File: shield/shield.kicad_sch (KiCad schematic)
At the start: 34 parts, among them Q1 Q_NMOS_DSG, Q2 Q_NMOS_DSG, U1 LM74900

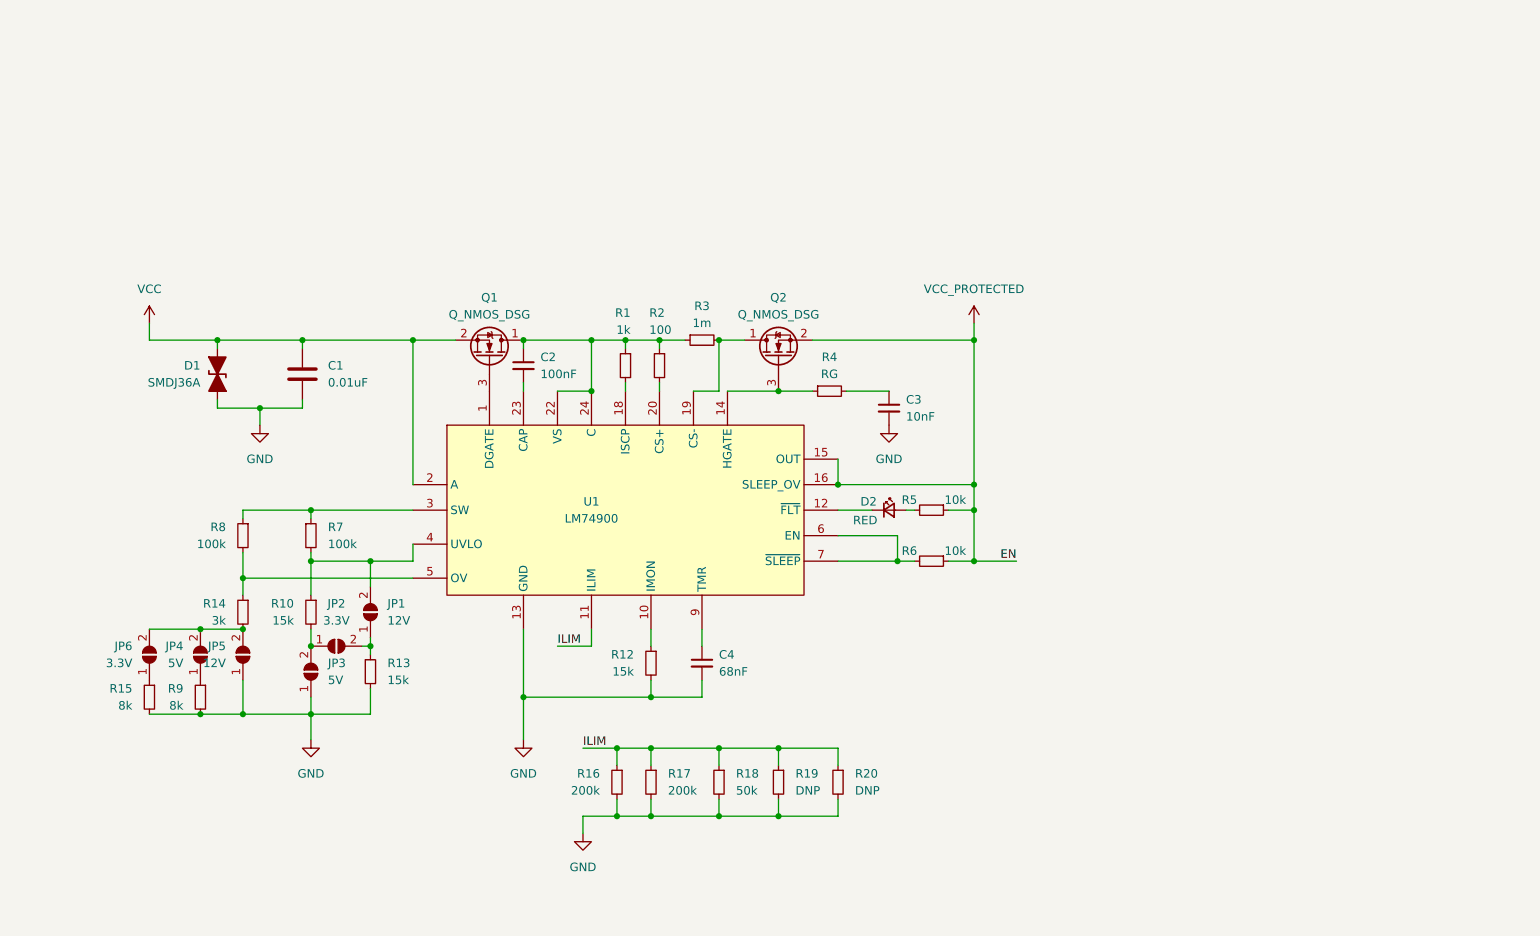
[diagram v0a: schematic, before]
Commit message: Feat[shield]: initial board layout + temporary footprints
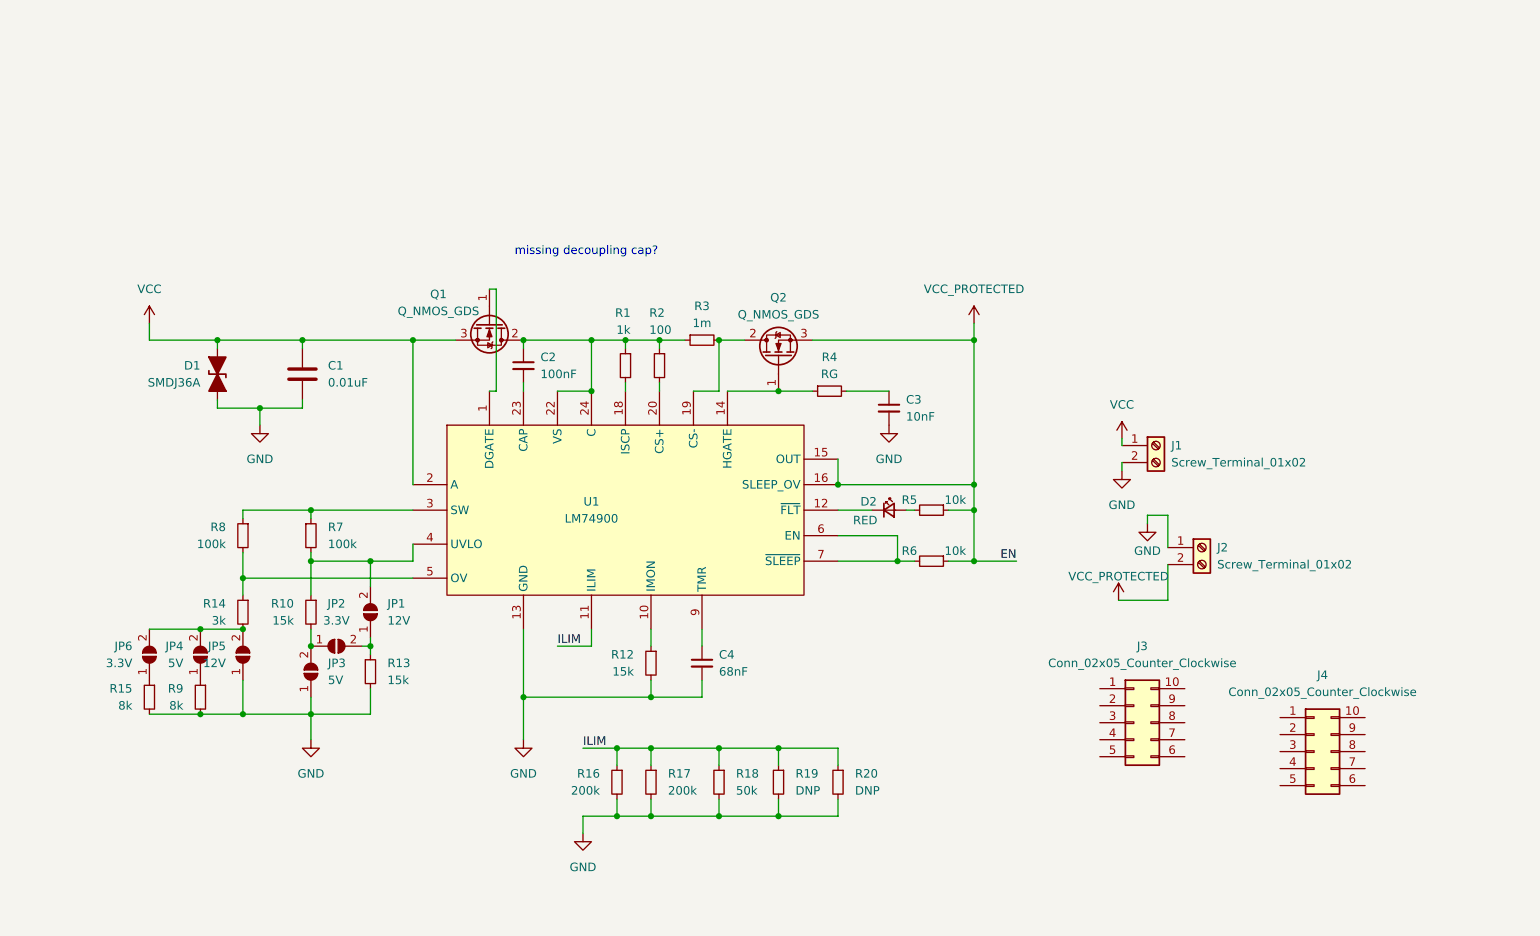
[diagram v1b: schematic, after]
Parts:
- removed Q1, Q2: Q_NMOS_DSG, symbol Device:Q_NMOS_DSG
- added J1, J2: Screw_Terminal_01x02, TerminalBlock_Phoenix:TerminalBlock_Phoenix_MKDS-1,5-2-5.08_1x02_P5.08mm_Horizontal, symbol Connector:Screw_Terminal_01x02
- added J3: Conn_02x05_Counter_Clockwise, DF40C-10:CONN_DF40B-10DS-0.4V51_HIR, symbol Connector_Generic:Conn_02x05_Counter_Clockwise
- added J4: Conn_02x05_Counter_Clockwise, DF40C-10:CONN_DF40C-10DP-0.4V51_HIR, symbol Connector_Generic:Conn_02x05_Counter_Clockwise
- added Q1, Q2: Q_NMOS_GDS, Package_TO_SOT_SMD:Infineon_PG-HSOF-8-1_ThermalVias, symbol Device:Q_NMOS_GDS
- C1, C2, C3, C4: footprint (none) -> Capacitor_SMD:C_0603_1608Metric
- D1: footprint (none) -> Diode_SMD:D_SMC
- D2: footprint (none) -> Diode_SMD:D_0603_1608Metric
- JP1, JP2, JP3, JP4, JP5, JP6: footprint (none) -> Jumper:SolderJumper-2_P1.3mm_Open_Pad1.0x1.5mm
- R1, R10, R12, R13, R14, R15, R16, R17, R18, R19, R2, R20, R4, R5, R6, R7, R8, R9: footprint (none) -> Resistor_SMD:R_0603_1608Metric
- R3: footprint (none) -> Resistor_SMD:R_2512_6332Metric
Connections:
- net GND: now also J1.2 (Pin_2), J2.1 (Pin_1)
- net VCC: now also J1.1 (Pin_1), Q1.3 (S)
- net VCC_PROTECTED: now also J2.2 (Pin_2), Q2.3 (S)
- net at C2.1, R1.1, R2.1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: now also Q1.2 (D)
- net at U1.1 (DGATE): now also Q1.1 (G)
- net at R3.2, U1.19 (CS-): now also Q2.2 (D)
- net at R4.1, U1.14 (HGATE): now also Q2.1 (G)
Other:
- note added: "missing decoupling cap?"

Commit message: Feat(shield): ready for routing
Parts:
- removed D2: RED, Diode_SMD:D_0603_1608Metric, symbol Device:LED_Small
- removed J3: Conn_02x05_Counter_Clockwise, DF40C-10:CONN_DF40B-10DS-0.4V51_HIR, symbol Connector_Generic:Conn_02x05_Counter_Clockwise
- removed J4: Conn_02x05_Counter_Clockwise, DF40C-10:CONN_DF40C-10DP-0.4V51_HIR, symbol Connector_Generic:Conn_02x05_Counter_Clockwise
- removed Q1, Q2: Q_NMOS_GDS, Package_TO_SOT_SMD:Infineon_PG-HSOF-8-1_ThermalVias, symbol Device:Q_NMOS_GDS
- added J3: IC Side 1, Connector_PinHeader_2.54mm:PinHeader_1x04_P2.54mm_Vertical, symbol Connector_Generic:Conn_01x04
- added J4: IC Side 2, Connector_PinHeader_2.54mm:PinHeader_1x04_P2.54mm_Vertical, symbol Connector_Generic:Conn_01x04
- added J5: Power Side 1, Connector_PinHeader_2.54mm:PinHeader_1x04_P2.54mm_Vertical, symbol Connector_Generic:Conn_01x04
- added J6: Power Side 2, Connector_PinHeader_2.54mm:PinHeader_1x04_P2.54mm_Vertical, symbol Connector_Generic:Conn_01x04
- added Q1, Q2: GAN3R2-100CBE, WLCSP8-SOT8072:WLCSP8-SOT8072, symbol NFET:Q_NMOS_GSD
- added TP1: ~{FLT}, TestPoint:TestPoint_Pad_1.0x1.0mm, symbol Connector:TestPoint_Small
- added TP2: EN, TestPoint:TestPoint_Pad_1.0x1.0mm, symbol Connector:TestPoint_Small
- added TP3: ~{SLEEP}, TestPoint:TestPoint_Pad_1.0x1.0mm, symbol Connector:TestPoint_Small
- C1: value 0.01uF -> 0.1uF; footprint Capacitor_SMD:C_0603_1608Metric -> Capacitor_SMD:C_1206_3216Metric
- JP1: value 12V -> 6
- JP2: value 3.3V -> 5
- JP3: value 5V -> 4
- JP4: value 5V -> 2
- JP5: value 12V -> 3
- JP6: value 3.3V -> 1
- R1, R10, R12, R13, R14, R15, R16, R17, R18, R2, R4, R5, R6, R7, R8, R9: footprint Resistor_SMD:R_0603_1608Metric -> Resistor_SMD:R_0402_1005Metric
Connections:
- net GND: now also J3.4 (Pin_4), J4.4 (Pin_4), J5.4 (Pin_4), J6.4 (Pin_4)
- net VCC: now also J5.1 (Pin_1), Q1.S; no longer U1.2 (A)
- net VCC_PROTECTED: now also J6.3 (Pin_3), Q2.S; no longer R5.1, R6.1, U1.15 (OUT), U1.16 (SLEEP_OV)
- net GATE1_IC: now reaches U1.1 (DGATE)
- net GATE1_IC: now also J3.2 (Pin_2)
- net SHUNT+_IC: now reaches C2.1, R1.1, R2.1, U1.22 (VS), U1.24 (C)
- net SHUNT+_IC: now also J3.3 (Pin_3); no longer R3.1
- net GATE2_IC: now reaches R4.1, U1.14 (HGATE)
- net GATE2_IC: now also J4.2 (Pin_2)
- net SHUNT-_IC: now reaches U1.19 (CS-)
- net SHUNT-_IC: now also J4.1 (Pin_1); no longer R3.2
- net at R6.2, U1.6 (EN), U1.7 (~{SLEEP}): now also TP2.1, TP3.1
- net at U1.12 (~{FLT}): now also R5.2, TP1.1
- new net EN: J4.3 (Pin_3), R5.1, R6.1, U1.15 (OUT), U1.16 (SLEEP_OV)
- new net GATE1_PWR: J5.2 (Pin_2), Q1.G
- new net GATE2_PWR: J6.2 (Pin_2), Q2.G
- new net SHUNT+_PWR: J5.3 (Pin_3), Q1.D, R3.1
- new net SHUNT-_PWR: J6.1 (Pin_1), Q2.D, R3.2
- new net VCC_IC: J3.1 (Pin_1), U1.2 (A)
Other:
- note added: "missing decoupling cap? - max"
- note added: "what do you mean? - byran"
- note removed: "missing decoupling cap?"
- moved on the sheet: C1, D1, J1, J2, R3

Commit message: Feat(shield): initial routing
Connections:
- net EN: now also J4.4 (Pin_4); no longer J4.3 (Pin_3)
- net GATE1_IC: now also J4.1 (Pin_1); no longer J3.2 (Pin_2)
- net GATE1_PWR: now also J6.1 (Pin_1); no longer J5.2 (Pin_2)
- net GATE2_IC: now also J3.3 (Pin_3); no longer J4.2 (Pin_2)
- net GATE2_PWR: now also J5.3 (Pin_3); no longer J6.2 (Pin_2)
- net GND: now also J3.2 (Pin_2), J5.2 (Pin_2); no longer J4.4 (Pin_4), J6.4 (Pin_4)
- net SHUNT+_IC: now also J4.2 (Pin_2); no longer J3.3 (Pin_3)
- net SHUNT+_PWR: now also J6.2 (Pin_2); no longer J5.3 (Pin_3)
- net SHUNT-_IC: now also J4.3 (Pin_3); no longer J4.1 (Pin_1)
- net SHUNT-_PWR: now also J6.3 (Pin_3); no longer J6.1 (Pin_1)
- net VCC_PROTECTED: now also J6.4 (Pin_4); no longer J6.3 (Pin_3)
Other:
- note added: "100nF for VS pin - Max"
- moved on the sheet: J4, J5
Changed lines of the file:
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@@
 	(wire
 		(pts
-			(xy 179.07 151.13) (xy 193.04 151.13)
+			(xy 179.07 137.16) (xy 193.04 137.16)
 		)
 		(stroke
@@
 	(wire
 		(pts
-			(xy 179.07 137.16) (xy 193.04 137.16)
+			(xy 179.07 156.972) (xy 193.04 156.972)
 		)
 		(stroke
@@
 	(wire
 		(pts
+			(xy 216.916 136.652) (xy 235.966 136.652)
+		)
+		(stroke
+			(width 0)
+			(type default)
+		)
+	)
+	(wire
+		(pts
 			(xy 88.9 134.62) (xy 88.9 133.35)
 		)
@@
 	(wire
 		(pts
-			(xy 212.09 151.13) (xy 227.33 151.13)
+			(xy 220.726 139.192) (xy 235.966 139.192)
 		)
 		(stroke
@@
 	(wire
 		(pts
-			(xy 212.09 148.59) (xy 227.33 148.59)
+			(xy 216.408 158.75) (xy 231.648 158.75)
 		)
 		(stroke
@@
 	(wire
 		(pts
-			(xy 212.09 137.16) (xy 227.33 137.16)
+			(xy 216.408 156.21) (xy 231.648 156.21)
 		)
 		(stroke
@@
 	(wire
 		(pts
-			(xy 212.09 153.67) (xy 227.33 153.67)
+			(xy 216.408 161.29) (xy 231.648 161.29)
 		)
 		(stroke
@@
 	(wire
 		(pts
-			(xy 212.09 134.62) (xy 227.33 134.62)
+			(xy 216.408 153.67) (xy 231.648 153.67)
 		)
 		(stroke
@@
 	(wire
 		(pts
-			(xy 179.07 148.59) (xy 193.04 148.59)
+			(xy 179.07 159.512) (xy 193.04 159.512)
 		)
 		(stroke
@@
 	(wire
 		(pts
+			(xy 172.974 134.62) (xy 193.04 134.62)
+		)
+		(stroke
+			(width 0)
+			(type default)
+		)
+	)
+	(wire
+		(pts
 			(xy 130.81 140.97) (xy 138.43 140.97)
 		)
@@
 	(wire
 		(pts
-			(xy 179.07 153.67) (xy 193.04 153.67)
+			(xy 179.07 162.052) (xy 193.04 162.052)
 		)
 		(stroke
@@
 	(wire
 		(pts
-			(xy 179.07 134.62) (xy 193.04 134.62)
+			(xy 179.07 154.432) (xy 193.04 154.432)
 		)
 		(stroke
@@
 	(wire
 		(pts
-			(xy 212.09 132.08) (xy 227.33 132.08)
+			(xy 220.726 134.112) (xy 235.966 134.112)
 		)
 		(stroke
@@
 		)
 	)
+	(text "100nF for VS pin - Max"
+		(exclude_from_sim no)
+		(at 106.426 52.07 0)
+		(effects
+			(font
+				(size 1.27 1.27)
+			)
+		)
+	)
 	(text "what do you mean? - byran"
 		(exclude_from_sim no)
@@
 	)
 	(label "SHUNT-_IC"
-		(at 179.07 148.59 0)
+		(at 179.07 159.512 0)
 		(fields_autoplaced yes)
 		(effects
@@
 	)
 	(label "GATE2_PWR"
-		(at 212.09 151.13 0)
+		(at 220.726 139.192 0)
 		(fields_autoplaced yes)
 		(effects
@@
 	)
 	(label "GATE2_IC"
-		(at 179.07 151.13 0)
+		(at 179.07 137.16 0)
 		(fields_autoplaced yes)
 		(effects
@@
 	)
 	(label "SHUNT+_PWR"
-		(at 212.09 137.16 0)
+		(at 216.408 156.21 0)
 		(fields_autoplaced yes)
 		(effects
@@
 	)
 	(label "VCC_PWR"
-		(at 212.09 132.08 0)
+		(at 220.726 134.112 0)
 		(fields_autoplaced yes)
 		(effects
@@
 	)
 	(label "GATE1_PWR"
-		(at 212.09 134.62 0)
+		(at 216.408 153.67 0)
 		(fields_autoplaced yes)
 		(effects
@@
 	)
 	(label "VCC_PROT_IC"
-		(at 179.07 153.67 0)
+		(at 179.07 162.052 0)
 		(fields_autoplaced yes)
 		(effects
@@
 	)
 	(label "SHUNT-_PWR"
-		(at 212.09 148.59 0)
+		(at 216.408 158.75 0)
 		(fields_autoplaced yes)
 		(effects
@@
 	)
 	(label "VCC_PROT_PWR"
-		(at 212.09 153.67 0)
+		(at 216.408 161.29 0)
 		(fields_autoplaced yes)
 		(effects
@@
 	)
 	(label "GATE1_IC"
-		(at 179.07 134.62 0)
+		(at 179.07 154.432 0)
 		(fields_autoplaced yes)
 		(effects
@@
 	)
 	(label "SHUNT+_IC"
-		(at 179.07 137.16 0)
+		(at 179.07 156.972 0)
 		(fields_autoplaced yes)
 		(effects
@@
 	(symbol
 		(lib_id "Connector_Generic:Conn_01x04")
-		(at 198.12 151.13 0)
+		(at 198.12 156.972 0)
 		(unit 1)
 		(exclude_from_sim no)
@@
 		(fields_autoplaced yes)
 		(property "Reference" "J4"
-			(at 200.66 151.1299 0)
+			(at 200.66 156.9719 0)
 			(effects
 				(font
@@
 		)
 		(property "Value" "IC Side 2"
-			(at 200.66 153.6699 0)
+			(at 200.66 159.5119 0)
 			(effects
 				(font
@@
 		)
 		(property "Footprint" "Connector_PinHeader_2.54mm:PinHeader_1x04_P2.54mm_Vertical"
-			(at 198.12 151.13 0)
+			(at 198.12 156.972 0)
 			(effects
 				(font
@@
 		)
 		(property "Datasheet" "~"
-			(at 198.12 151.13 0)
+			(at 198.12 156.972 0)
 			(effects
 				(font
@@
 		)
 		(property "Description" "Generic connector, single row, 01x04, script generated (kicad-library-utils/schlib/autogen/connector/)"
-			(at 198.12 151.13 0)
+			(at 198.12 156.972 0)
 			(effects
 				(font
@@
 	(symbol
 		(lib_id "Connector_Generic:Conn_01x04")
-		(at 232.41 151.13 0)
+		(at 236.728 156.21 0)
 		(unit 1)
 		(exclude_from_sim no)
@@
 		(fields_autoplaced yes)
 		(property "Reference" "J6"
-			(at 234.95 151.1299 0)
+			(at 239.268 156.2099 0)
 			(effects
 				(font
@@
 		)
 		(property "Value" "Power Side 2"
-			(at 234.95 153.6699 0)
+			(at 239.268 158.7499 0)
 			(effects
 				(font
@@
 		)
 		(property "Footprint" "Connector_PinHeader_2.54mm:PinHeader_1x04_P2.54mm_Vertical"
-			(at 232.41 151.13 0)
+			(at 236.728 156.21 0)
 			(effects
 				(font
@@
 		)
 		(property "Datasheet" "~"
-			(at 232.41 151.13 0)
+			(at 236.728 156.21 0)
 			(effects
 				(font
@@
 		)
 		(property "Description" "Generic connector, single row, 01x04, script generated (kicad-library-utils/schlib/autogen/connector/)"
-			(at 232.41 151.13 0)
+			(at 236.728 156.21 0)
 			(effects
 				(font
@@
 	(symbol
 		(lib_id "Connector_Generic:Conn_01x04")
-		(at 232.41 134.62 0)
+		(at 241.046 136.652 0)
 		(unit 1)
 		(exclude_from_sim no)
@@
 		(fields_autoplaced yes)
 		(property "Reference" "J5"
-			(at 234.95 134.6199 0)
+			(at 243.586 136.6519 0)
 			(effects
 				(font
@@
 		)
 		(property "Value" "Power Side 1"
-			(at 234.95 137.1599 0)
+			(at 243.586 139.1919 0)
 			(effects
 				(font
@@
 		)
 		(property "Footprint" "Connector_PinHeader_2.54mm:PinHeader_1x04_P2.54mm_Vertical"
-			(at 232.41 134.62 0)
+			(at 241.046 136.652 0)
 			(effects
 				(font
@@
 		)
 		(property "Datasheet" "~"
-			(at 232.41 134.62 0)
+			(at 241.046 136.652 0)
 			(effects
 				(font
@@
 		)
 		(property "Description" "Generic connector, single row, 01x04, script generated (kicad-library-utils/schlib/autogen/connector/)"
-			(at 232.41 134.62 0)
+			(at 241.046 136.652 0)
 			(effects
 				(font
@@
 	(symbol
 		(lib_id "power:GND")
-		(at 227.33 156.21 0)
+		(at 216.916 136.652 0)
 		(unit 1)
 		(exclude_from_sim no)
@@
 		(dnp no)
 		(property "Reference" "#PWR015"
-			(at 227.33 162.56 0)
+			(at 216.916 143.002 0)
 			(effects
 				(font
@@
 		)
 		(property "Value" "GND"
-			(at 227.33 160.274 0)
+			(at 216.916 140.716 0)
 			(effects
 				(font
@@
 		)
 		(property "Footprint" ""
-			(at 227.33 156.21 0)
+			(at 216.916 136.652 0)
 			(effects
 				(font
@@
 		)
 		(property "Datasheet" ""
-			(at 227.33 156.21 0)
+			(at 216.916 136.652 0)
 			(effects
 				(font
@@
 		)
 		(property "Description" "Power symbol creates a global label with name \"GND\" , ground"
-			(at 227.33 156.21 0)
+			(at 216.916 136.652 0)
 			(effects
 				(font
@@
 	(symbol
 		(lib_id "power:GND")
-		(at 227.33 139.7 0)
+		(at 235.966 141.732 0)
 		(unit 1)
 		(exclude_from_sim no)
@@
 		(dnp no)
 		(property "Reference" "#PWR013"
-			(at 227.33 146.05 0)
+			(at 235.966 148.082 0)
 			(effects
 				(font
@@
 		)
 		(property "Value" "GND"
-			(at 227.33 143.764 0)
+			(at 235.966 145.796 0)
 			(effects
 				(font
@@
 		)
 		(property "Footprint" ""
-			(at 227.33 139.7 0)
+			(at 235.966 141.732 0)
 			(effects
 				(font
@@
 		)
 		(property "Datasheet" ""
-			(at 227.33 139.7 0)
+			(at 235.966 141.732 0)
 			(effects
 				(font
@@
 		)
 		(property "Description" "Power symbol creates a global label with name \"GND\" , ground"
-			(at 227.33 139.7 0)
+			(at 235.966 141.732 0)
 			(effects
 				(font
@@
 	(symbol
 		(lib_id "power:GND")
-		(at 193.04 156.21 0)
+		(at 172.974 134.62 0)
 		(unit 1)
 		(exclude_from_sim no)
@@
 		(dnp no)
 		(property "Reference" "#PWR014"
-			(at 193.04 162.56 0)
+			(at 172.974 140.97 0)
 			(effects
 				(font
@@
 		)
 		(property "Value" "GND"
-			(at 193.04 160.274 0)
+			(at 172.974 138.684 0)
 			(effects
 				(font
@@
 		)
 		(property "Footprint" ""
-			(at 193.04 156.21 0)
+			(at 172.974 134.62 0)
 			(effects
 				(font
@@
 		)
 		(property "Datasheet" ""
-			(at 193.04 156.21 0)
+			(at 172.974 134.62 0)
 			(effects
 				(font
@@
 		)
 		(property "Description" "Power symbol creates a global label with name \"GND\" , ground"
-			(at 193.04 156.21 0)
+			(at 172.974 134.62 0)
 			(effects
 				(font
